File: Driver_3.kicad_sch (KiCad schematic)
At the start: 32 parts

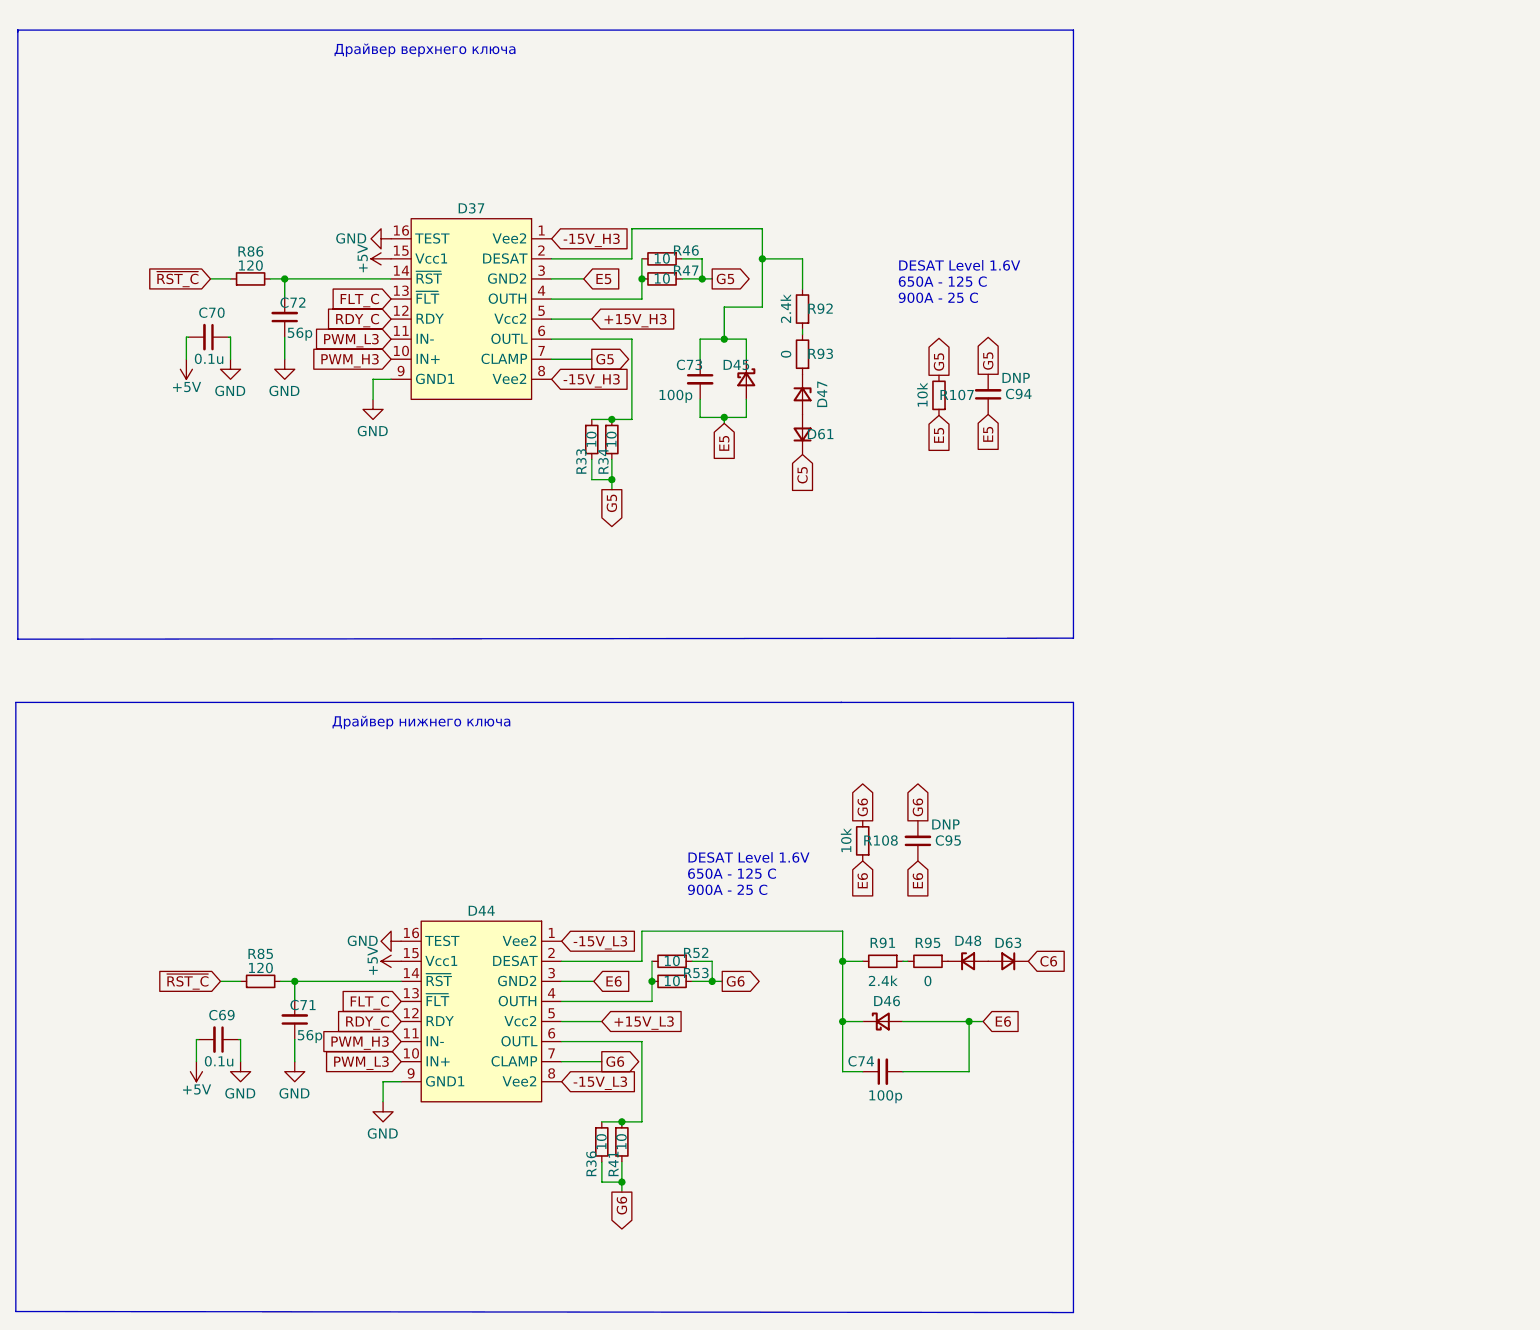
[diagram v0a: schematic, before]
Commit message: VER2.2: добавил фильтры на вход ШИМа и обновил все доки
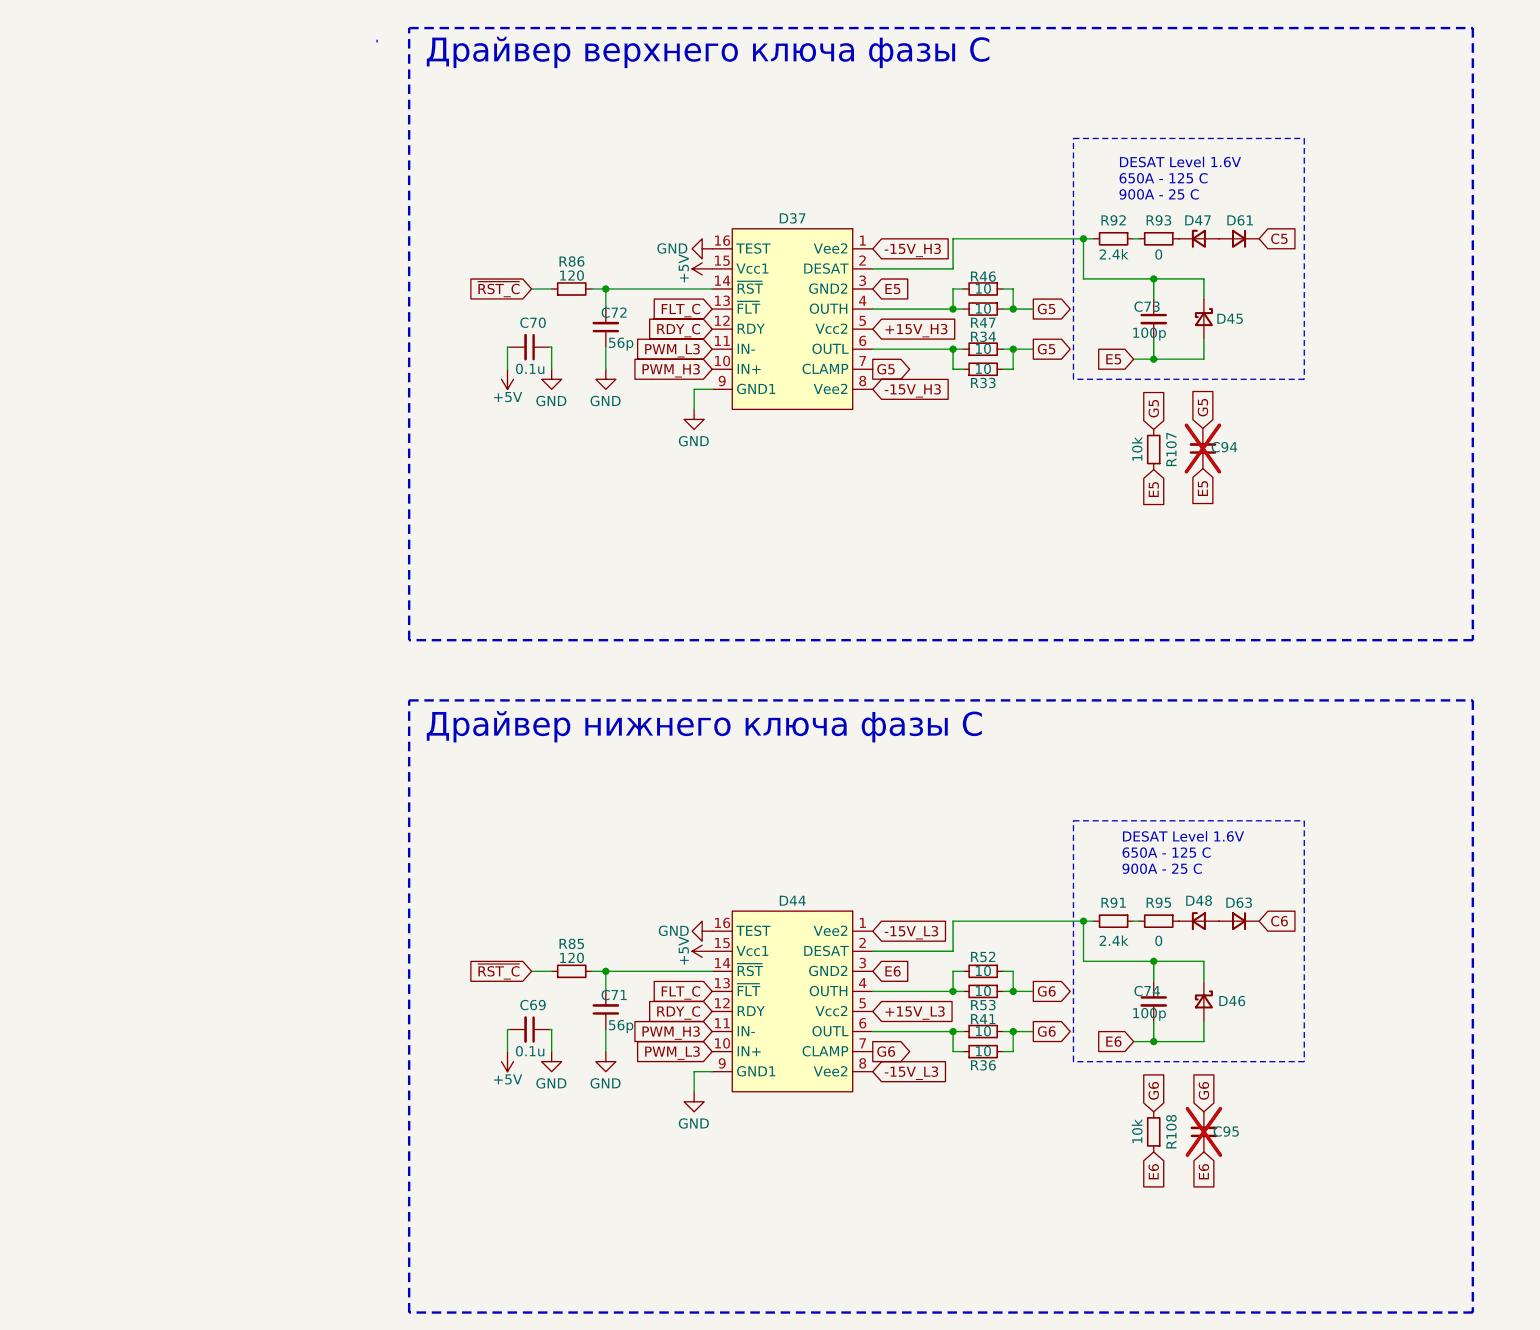
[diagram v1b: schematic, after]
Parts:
- C94, C95: value DNP -> ~; now not fitted
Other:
- note added: "Драйвер верхнего ключа фазы С"
- note added: "Драйвер нижнего ключа фазы С"
- note removed: "Драйвер верхнего ключа"
- note removed: "Драйвер нижнего ключа"
- company: (none) -> ООО "ЭТТ"
- moved on the sheet: C69, C70, C71, C72, C73, C74, D37, D44, D45, D46, D47, D48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

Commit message: VER2.2.1: исправил косяк с питанием NTC, изменил номиналы затворов и цепи NTC
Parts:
- R46, R47, R52, R53: value 10 -> 6.8
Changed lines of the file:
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@@
 			)
 		)
-		(property "Value" "10"
+		(property "Value" "6.8"
 			(at 153.67 142.24 90)
 			(effects
@@
 			)
 		)
-		(property "Value" "10"
+		(property "Value" "6.8"
 			(at 153.67 58.42 90)
 			(effects
@@
 			)
 		)
-		(property "Value" "10"
+		(property "Value" "6.8"
 			(at 153.67 144.78 90)
 			(effects
@@
 			)
 		)
-		(property "Value" "10"
+		(property "Value" "6.8"
 			(at 153.67 55.88 90)
 			(effects

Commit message: VER2.2.1: создал папку для производственных доков
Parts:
- C69, C70, C71, C72, C73, C74, C94, C95: Description P/N (none) -> Capacitor SMD 25+V
- R107, R108, R33, R34, R36, R41, R46, R47, R52, R53, R85, R86, R91, R92, R93, R95: Description P/N (none) -> Resistor SMD
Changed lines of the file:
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@@
 			)
 		)
-		(property "Description P/N" ""
+		(property "Description P/N" "Capacitor SMD 25+V"
 			(at 181.61 162.56 0)
 			(effects
@@
 			)
 		)
-		(property "Description P/N" ""
+		(property "Description P/N" "Resistor SMD"
 			(at 153.67 152.4 0)
 			(effects
@@
 			)
 		)
-		(property "Description P/N" ""
+		(property "Description P/N" "Capacitor SMD 25+V"
 			(at 105.918 60.706 0)
 			(effects
@@
 			)
 		)
-		(property "Description P/N" ""
+		(property "Description P/N" "Resistor SMD"
 			(at 153.67 149.86 0)
 			(effects
@@
 			)
 		)
-		(property "Description P/N" ""
+		(property "Description P/N" "Capacitor SMD 25+V"
 			(at 105.918 147.066 0)
 			(effects
@@
 			)
 		)
-		(property "Description P/N" ""
+		(property "Description P/N" "Resistor SMD"
 			(at 175.26 162.56 0)
 			(effects
@@
 			)
 		)
-		(property "Description P/N" ""
+		(property "Description P/N" "Capacitor SMD 25+V"
 			(at 175.26 59.69 0)
 			(effects
@@
 			)
 		)
-		(property "Description P/N" ""
+		(property "Description P/N" "Resistor SMD"
 			(at 153.67 66.04 0)
 			(effects
@@
 			)
 		)
-		(property "Description P/N" ""
+		(property "Description P/N" "Resistor SMD"
 			(at 170.18 135.89 0)
 			(effects
@@
 			)
 		)
-		(property "Description P/N" ""
+		(property "Description P/N" "Resistor SMD"
 			(at 175.26 76.2 0)
 			(effects
@@
 			)
 		)
-		(property "Description P/N" ""
+		(property "Description P/N" "Capacitor SMD 25+V"
 			(at 181.483 76.073 0)
 			(effects
@@
 			)
 		)
-		(property "Description P/N" ""
+		(property "Description P/N" "Resistor SMD"
 			(at 175.895 49.53 0)
 			(effects
@@
 			)
 		)
-		(property "Description P/N" ""
+		(property "Description P/N" "Resistor SMD"
 			(at 153.67 142.24 0)
 			(effects
@@
 			)
 		)
-		(property "Description P/N" ""
+		(property "Description P/N" "Resistor SMD"
 			(at 101.6 142.24 0)
 			(effects
@@
 			)
 		)
-		(property "Description P/N" ""
+		(property "Description P/N" "Capacitor SMD 25+V"
 			(at 175.26 146.05 0)
 			(effects
@@
 			)
 		)
-		(property "Description P/N" ""
+		(property "Description P/N" "Resistor SMD"
 			(at 153.67 58.42 0)
 			(effects
@@
 			)
 		)
-		(property "Description P/N" ""
+		(property "Description P/N" "Resistor SMD"
 			(at 153.67 63.5 0)
 			(effects
@@
 			)
 		)
-		(property "Description P/N" ""
+		(property "Description P/N" "Resistor SMD"
 			(at 153.67 144.78 0)
 			(effects
@@
 			)
 		)
-		(property "Description P/N" ""
+		(property "Description P/N" "Resistor SMD"
 			(at 170.18 49.53 0)
 			(effects
@@
 			)
 		)
-		(property "Description P/N" ""
+		(property "Description P/N" "Resistor SMD"
 			(at 101.6 55.88 0)
 			(effects
@@
 			)
 		)
-		(property "Description P/N" ""
+		(property "Description P/N" "Resistor SMD"
 			(at 175.895 135.89 0)
 			(effects
@@
 			)
 		)
-		(property "Description P/N" ""
+		(property "Description P/N" "Capacitor SMD 25+V"
 			(at 96.266 149.606 0)
 			(effects
@@
 			)
 		)
-		(property "Description P/N" ""
+		(property "Description P/N" "Capacitor SMD 25+V"
 			(at 96.266 63.246 0)
 			(effects
@@
 			)
 		)
-		(property "Description P/N" ""
+		(property "Description P/N" "Resistor SMD"
 			(at 153.67 55.88 0)
 			(effects

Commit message: VER2.2.1: исправил все доки
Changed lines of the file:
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@@
 		(date "2025-06-04")
 		(company "ООО \"ЭТТ\"")
+		(comment 1 "НВЦТ.EVP150-2-1.2000.120_v1 Э3")
 	)
 	(rectangle
@@
 				)
 				(justify left)
+				(hide yes)
 			)
 		)
@@
 					(size 1.27 1.27)
 				)
+				(hide yes)
 			)
 		)
@@
 					(size 1.27 1.27)
 				)
+				(hide yes)
 			)
 		)
@@
 					(size 1.27 1.27)
 				)
+				(hide yes)
 			)
 		)
@@
 					(size 1.27 1.27)
 				)
+				(hide yes)
 			)
 		)
@@
 					(size 1.27 1.27)
 				)
+				(hide yes)
 			)
 		)
@@
 					(size 1.27 1.27)
 				)
+				(hide yes)
 			)
 		)
@@
 					(size 1.27 1.27)
 				)
+				(hide yes)
 			)
 		)
@@
 					(size 1.27 1.27)
 				)
+				(hide yes)
 			)
 		)
@@
 					(size 1.27 1.27)
 				)
+				(hide yes)
 			)
 		)
@@
 					(size 1.27 1.27)
 				)
+				(hide yes)
 			)
 		)
@@
 				)
 				(justify left)
+				(hide yes)
 			)
 		)
@@
 					(size 1.27 1.27)
 				)
+				(hide yes)
 			)
 		)
@@
 					(size 1.27 1.27)
 				)
+				(hide yes)
 			)
 		)
@@
 					(size 1.27 1.27)
 				)
+				(hide yes)
 			)
 		)
@@
 					(size 1.27 1.27)
 				)
+				(hide yes)
 			)
 		)
@@
 					(size 1.27 1.27)
 				)
+				(hide yes)
 			)
 		)
@@
 					(size 1.27 1.27)
 				)
+				(hide yes)
 			)
 		)
@@
 					(size 1.27 1.27)
 				)
+				(hide yes)
 			)
 		)
@@
 					(size 1.27 1.27)
 				)
+				(hide yes)
 			)
 		)
@@
 					(size 1.27 1.27)
 				)
+				(hide yes)
 			)
 		)
@@
 					(size 1.27 1.27)
 				)
+				(hide yes)
 			)
 		)
@@
 					(size 1.27 1.27)
 				)
+				(hide yes)
 			)
 		)
@@
 					(size 1.27 1.27)
 				)
+				(hide yes)
 			)
 		)
@@
 					(size 1.27 1.27)
 				)
+				(hide yes)
 			)
 		)
@@
 					(size 1.27 1.27)
 				)
+				(hide yes)
 			)
 		)

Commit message: VER2.2: исправил ошибки в доках
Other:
- moved on the sheet: C69, C70, C71, C72, C73, C74, C94, C95, D37, D44, D45, D46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
